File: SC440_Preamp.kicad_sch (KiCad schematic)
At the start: 24 parts, among them J1 JST-XH 1x04 TO DIGITAL BOARD, J2 ANALOG BOARD, U1 OPA1678IDR

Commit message: fix spice tool and pin assignments
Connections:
- net +5V: now also VCCSIM1.1 (+); no longer VCCSIM1.2 (-)
- net ANALOG_INPUT: now also VTEST1.1 (+); no longer VTEST1.2 (-)
- net FB: now also XAMP1.4 (-IN); no longer XAMP1.3 (+IN)
- net GND: now also VCCSIM1.2 (-), VTEST1.2 (-), XAMP1.2 (VEE), XREF1.2 (VEE); no longer VCCSIM1.1 (+), VTEST1.1 (+), XAMP1.1 (OUT), XREF1.1 (OUT)
- net IN_AC: now also XAMP1.3 (+IN); no longer XAMP1.4 (-IN)
- net PREAMP_OUT: now also XAMP1.1 (OUT); no longer XAMP1.2 (VEE)
- net VREF: now also XREF1.1 (OUT), XREF1.4 (-IN); no longer XREF1.2 (VEE), XREF1.3 (+IN)
- net VREF_RAW: now also XREF1.3 (+IN); no longer XREF1.4 (-IN)
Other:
- moved on the sheet: VCCSIM1, VTEST1
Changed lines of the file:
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@@
 	(wire
 		(pts
-			(xy 135.08 211.27) (xy 143 211.27)
+			(xy 142.365 212.54) (xy 144.27 212.54)
+		)
+		(stroke
+			(width 0)
+			(type solid)
+		)
+	)
+	(wire
+		(pts
+			(xy 142.365 211.27) (xy 135.08 211.27)
 		)
 		(stroke
@@
 	(wire
 		(pts
+			(xy 192.365 212.54) (xy 192.365 211.27)
+		)
+		(stroke
+			(width 0)
+			(type solid)
+		)
+	)
+	(wire
+		(pts
 			(xy 26.67 56.64) (xy 26.67 113.792)
 		)
@@
 	(wire
 		(pts
+			(xy 192.365 211.27) (xy 185.08 211.27)
+		)
+		(stroke
+			(width 0)
+			(type solid)
+		)
+	)
+	(wire
+		(pts
 			(xy 165.862 85.09) (xy 176.53 85.09)
 		)
@@
 	(wire
 		(pts
+			(xy 142.365 212.54) (xy 142.365 211.27)
+		)
+		(stroke
+			(width 0)
+			(type solid)
+		)
+	)
+	(wire
+		(pts
 			(xy 42.545 48.385) (xy 34.29 48.385)
 		)
@@
 	(wire
 		(pts
-			(xy 185.08 211.27) (xy 193 211.27)
+			(xy 192.365 212.54) (xy 194.27 212.54)
 		)
 		(stroke
@@
 	)
 	(label "VREF"
-		(at 193 208.73 0)
+		(at 194.27 212.54 0)
 		(effects
 			(font
@@
 	)
 	(label "IN_AC"
-		(at 117 208.73 180)
+		(at 117 211.27 180)
 		(effects
 			(font
@@
 	)
 	(label "VREF"
-		(at 167 211.27 180)
+		(at 167 208.73 180)
 		(effects
 			(font
@@
 	)
 	(label "PREAMP_OUT"
-		(at 143 208.73 0)
+		(at 144.27 212.54 0)
 		(effects
 			(font
@@
 	)
 	(label "VREF_RAW"
-		(at 167 208.73 180)
+		(at 167 211.27 180)
 		(effects
 			(font
@@
 	)
 	(label "FB"
-		(at 117 211.27 180)
+		(at 117 208.73 180)
 		(effects
 			(font
@@
 			)
 		)
-		(property "Sim.Pins" "1=4 2=5 3=2 4=1 5=3"
+		(property "Sim.Pins" "1=OUT 2=VEE 3=IN+ 4=IN- 5=VCC"
 			(at 0 0 0)
 			(hide yes)
@@
 			)
 		)
-		(property "Sim.Pins" "1=4 2=5 3=2 4=1 5=3"
+		(property "Sim.Pins" "1=OUT 2=VEE 3=IN+ 4=IN- 5=VCC"
 			(at 0 0 0)
 			(hide yes)
@@
 	(symbol
 		(lib_id "power:GND")
-		(at 193 211.27 0)
+		(at 193 208.73 90)
 		(unit 1)
 		(body_style 1)
@@
 		(fields_autoplaced yes)
 		(property "Reference" "#PWR012"
-			(at 193 217.62 0)
+			(at 199.35 208.73 0)
 			(hide yes)
 			(show_name no)
@@
 		)
 		(property "Value" "GND"
-			(at 195.58 212.5399 0)
+			(at 196.85 208.7299 90)
 			(show_name no)
 			(do_not_autoplace no)
@@
 					(size 1.27 1.27)
 				)
-				(justify left)
+				(justify right)
 			)
 		)
 		(property "Footprint" ""
-			(at 193 211.27 0)
+			(at 193 208.73 0)
 			(hide yes)
 			(show_name no)
@@
 		)
 		(property "Datasheet" ""
-			(at 193 211.27 0)
+			(at 193 208.73 0)
 			(hide yes)
 			(show_name no)
@@
 		)
 		(property "Description" "Power symbol creates a global label with name \"GND\" , ground"
-			(at 193 211.27 0)
+			(at 193 208.73 0)
 			(hide yes)
 			(show_name no)
@@
 	(symbol
 		(lib_id "power:GND")
-		(at 143 211.27 0)
+		(at 143 208.73 90)
 		(unit 1)
 		(body_style 1)
@@
 		(fields_autoplaced yes)
 		(property "Reference" "#PWR011"
-			(at 143 217.62 0)
+			(at 149.35 208.73 0)
 			(hide yes)
 			(show_name no)
@@
 		)
 		(property "Value" "GND"
-			(at 146.05 212.5399 0)
+			(at 147.32 208.7299 90)
 			(show_name no)
 			(do_not_autoplace no)
@@
 					(size 1.27 1.27)
 				)
-				(justify left)
+				(justify right)
 			)
 		)
 		(property "Footprint" ""
-			(at 143 211.27 0)
+			(at 143 208.73 0)
 			(hide yes)
 			(show_name no)
@@
 		)
 		(property "Datasheet" ""
-			(at 143 211.27 0)
+			(at 143 208.73 0)
 			(hide yes)
 			(show_name no)
@@
 		)
 		(property "Description" "Power symbol creates a global label with name \"GND\" , ground"
-			(at 143 211.27 0)
+			(at 143 208.73 0)
 			(hide yes)
 			(show_name no)
@@
 	(symbol
 		(lib_id "SC440_Preamp:VDC")
-		(at 75 210 0)
+		(at 75 210 180)
 		(unit 1)
 		(body_style 1)
@@
 					(size 1.27 1.27)
 				)
-				(justify left)
+				(justify right)
 			)
 		)
@@
 					(size 1.27 1.27)
 				)
-				(justify left)
+				(justify right)
 			)
 		)
 		(property "Footprint" ""
-			(at 75 211 0)
+			(at 75 209 0)
 			(hide yes)
 			(show_name no)
@@
 		)
 		(property "Datasheet" ""
-			(at 75 213 0)
+			(at 75 207 0)
 			(hide yes)
 			(show_name no)
@@
 			)
 		)
-		(property "Sim.Pins" "1=- 2=+"
-			(at 0 0 0)
+		(property "Sim.Pins" "1=+ 2=-"
+			(at 150 420 0)
 			(hide yes)
 			(show_name no)
@@
 		)
 		(property "Sim.Device" "V"
-			(at 0 0 0)
+			(at 150 420 0)
 			(hide yes)
 			(show_name no)
@@
 		)
 		(property "Sim.Type" "DC"
-			(at 0 0 0)
+			(at 150 420 0)
 			(hide yes)
 			(show_name no)
@@
 		)
 		(property "Sim.Params" "dc=5"
-			(at 0 0 0)
+			(at 150 420 0)
 			(hide yes)
 			(show_name no)
@@
 	(symbol
 		(lib_id "SC440_Preamp:VSIN")
-		(at 45 210 0)
+		(at 45 210 180)
 		(unit 1)
 		(body_style 1)
@@
 					(size 1.27 1.27)
 				)
-				(justify left)
+				(justify right)
 			)
 		)
@@
 					(size 1.27 1.27)
 				)
-				(justify left)
+				(justify right)
 			)
 		)
 		(property "Footprint" ""
-			(at 45 211 0)
+			(at 45 209 0)
 			(hide yes)
 			(show_name no)
@@
 		)
 		(property "Datasheet" ""
-			(at 45 213 0)
+			(at 45 207 0)
 			(hide yes)
 			(show_name no)
@@
 			)
 		)
-		(property "Sim.Pins" "1=- 2=+"
-			(at 0 0 0)
+		(property "Sim.Pins" "1=+ 2=-"
+			(at 90 420 0)
 			(hide yes)
 			(show_name no)
@@
 		)
 		(property "Sim.Device" "V"
-			(at 0 0 0)
+			(at 90 420 0)
 			(hide yes)
 			(show_name no)
@@
 		)
 		(property "Sim.Type" "SIN"
-			(at 0 0 0)
+			(at 90 420 0)
 			(hide yes)
 			(show_name no)
@@
 		)
 		(property "Sim.Params" "dc=2.426 ampl=10m f=1k ac=1"
-			(at 0 0 0)
+			(at 90 420 0)
 			(hide yes)
 			(show_name no)

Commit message: ...
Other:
- moved on the sheet: J2, XAMP1, XREF1

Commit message: add input and output filter
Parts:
- added C5: 330p, Capacitor_SMD:C_0805_2012Metric_Pad1.18x1.45mm_HandSolder, symbol SC440_Preamp:C
- added C7: 1n, Capacitor_SMD:C_0805_2012Metric_Pad1.18x1.45mm_HandSolder, symbol SC440_Preamp:C
- added R4: 1k, Resistor_SMD:R_0805_2012Metric_Pad1.20x1.40mm_HandSolder, symbol SC440_Preamp:R
- R8: now not fitted
- R8: renamed from R10; now fitted
- renumbered C5 to C6, C6 to C8, R11 to R10, R4 to R2, R2 to R5, R5 to R6, R6 to R9
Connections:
- net ANALOG_OUTPUT: now also C7.1
- net GND: now also C5.2, C7.2
- net IN_AC: now also C5.1, R4.2; no longer C2.2, R2.2
- new net: C2.2, R2.2, R4.1

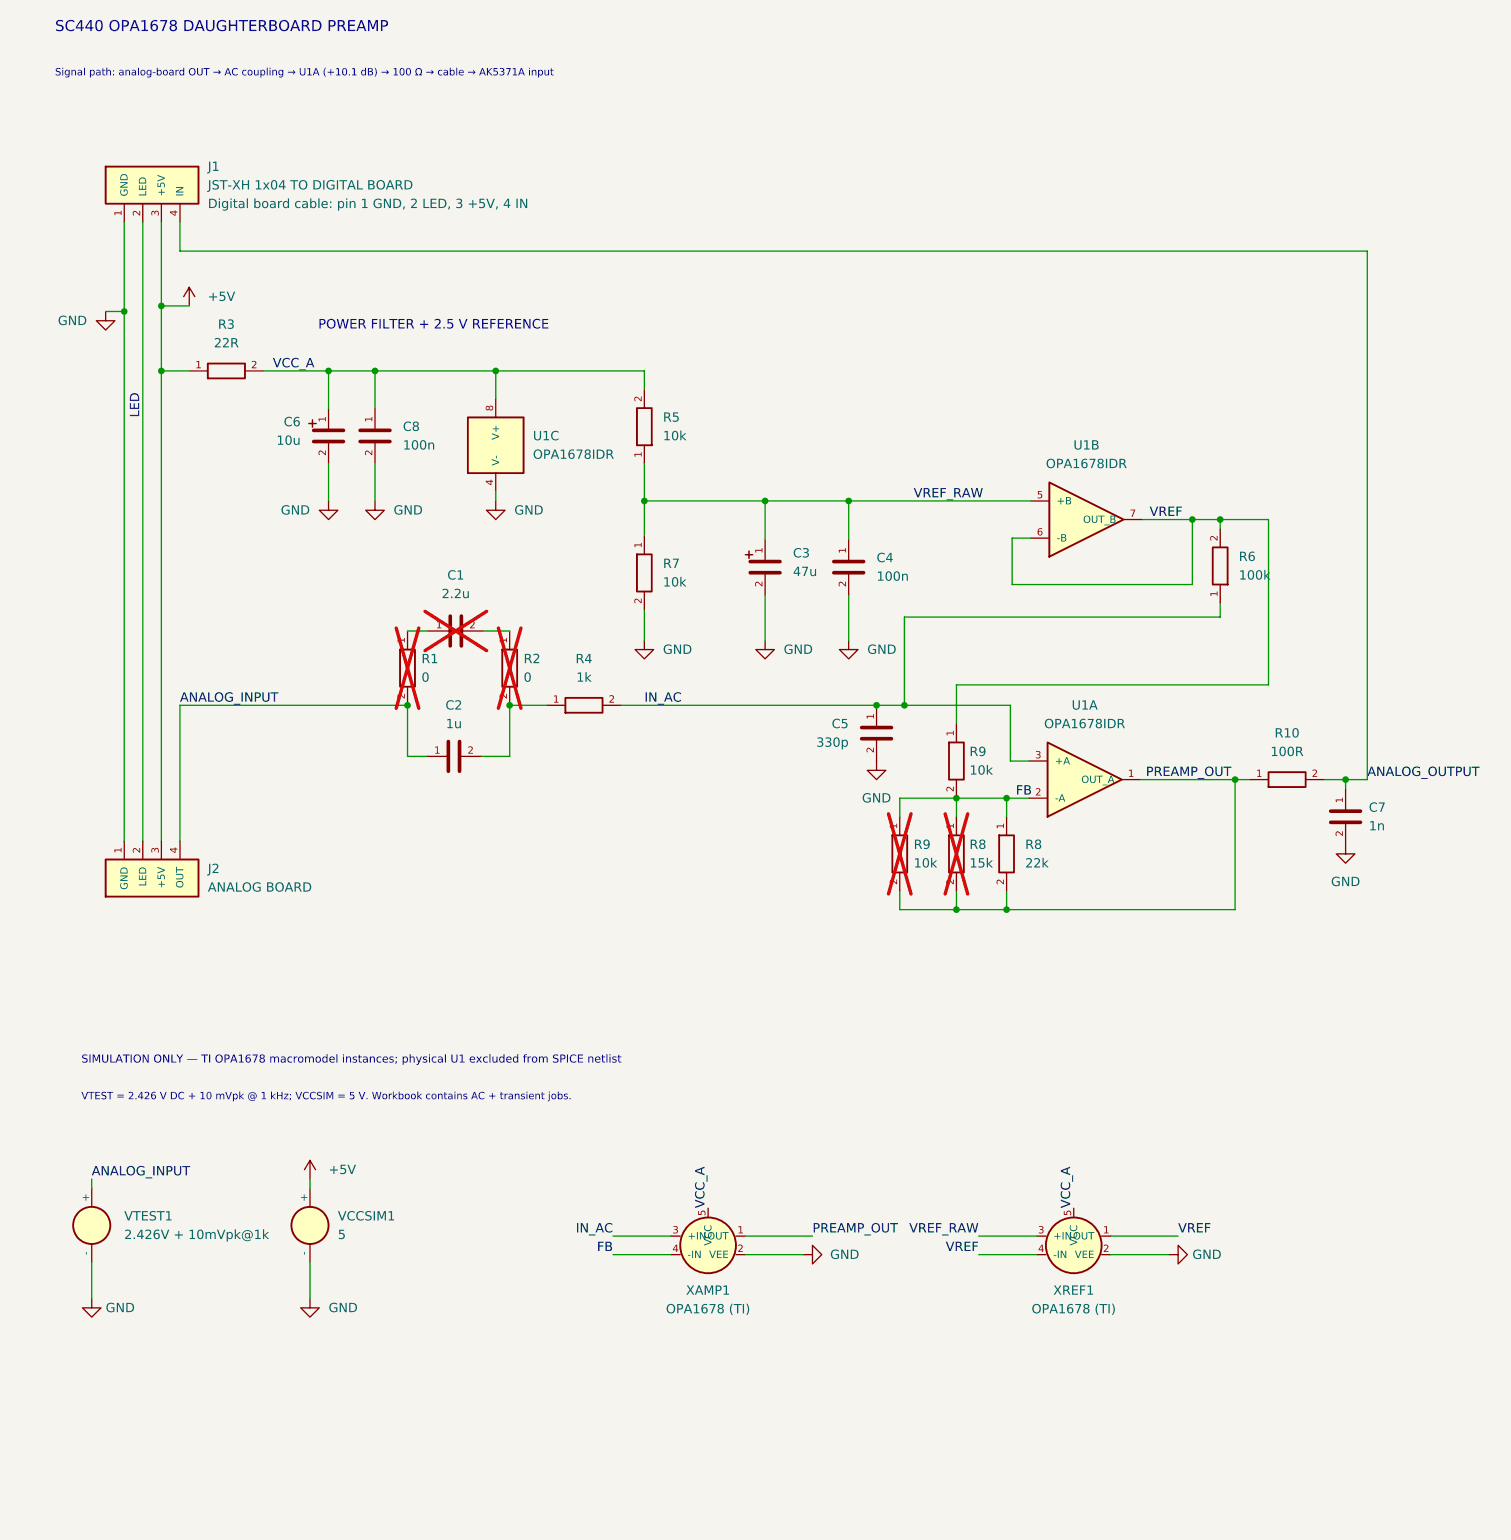
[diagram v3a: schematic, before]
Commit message: add more filtering, silkscreen, pinsockets as spacers
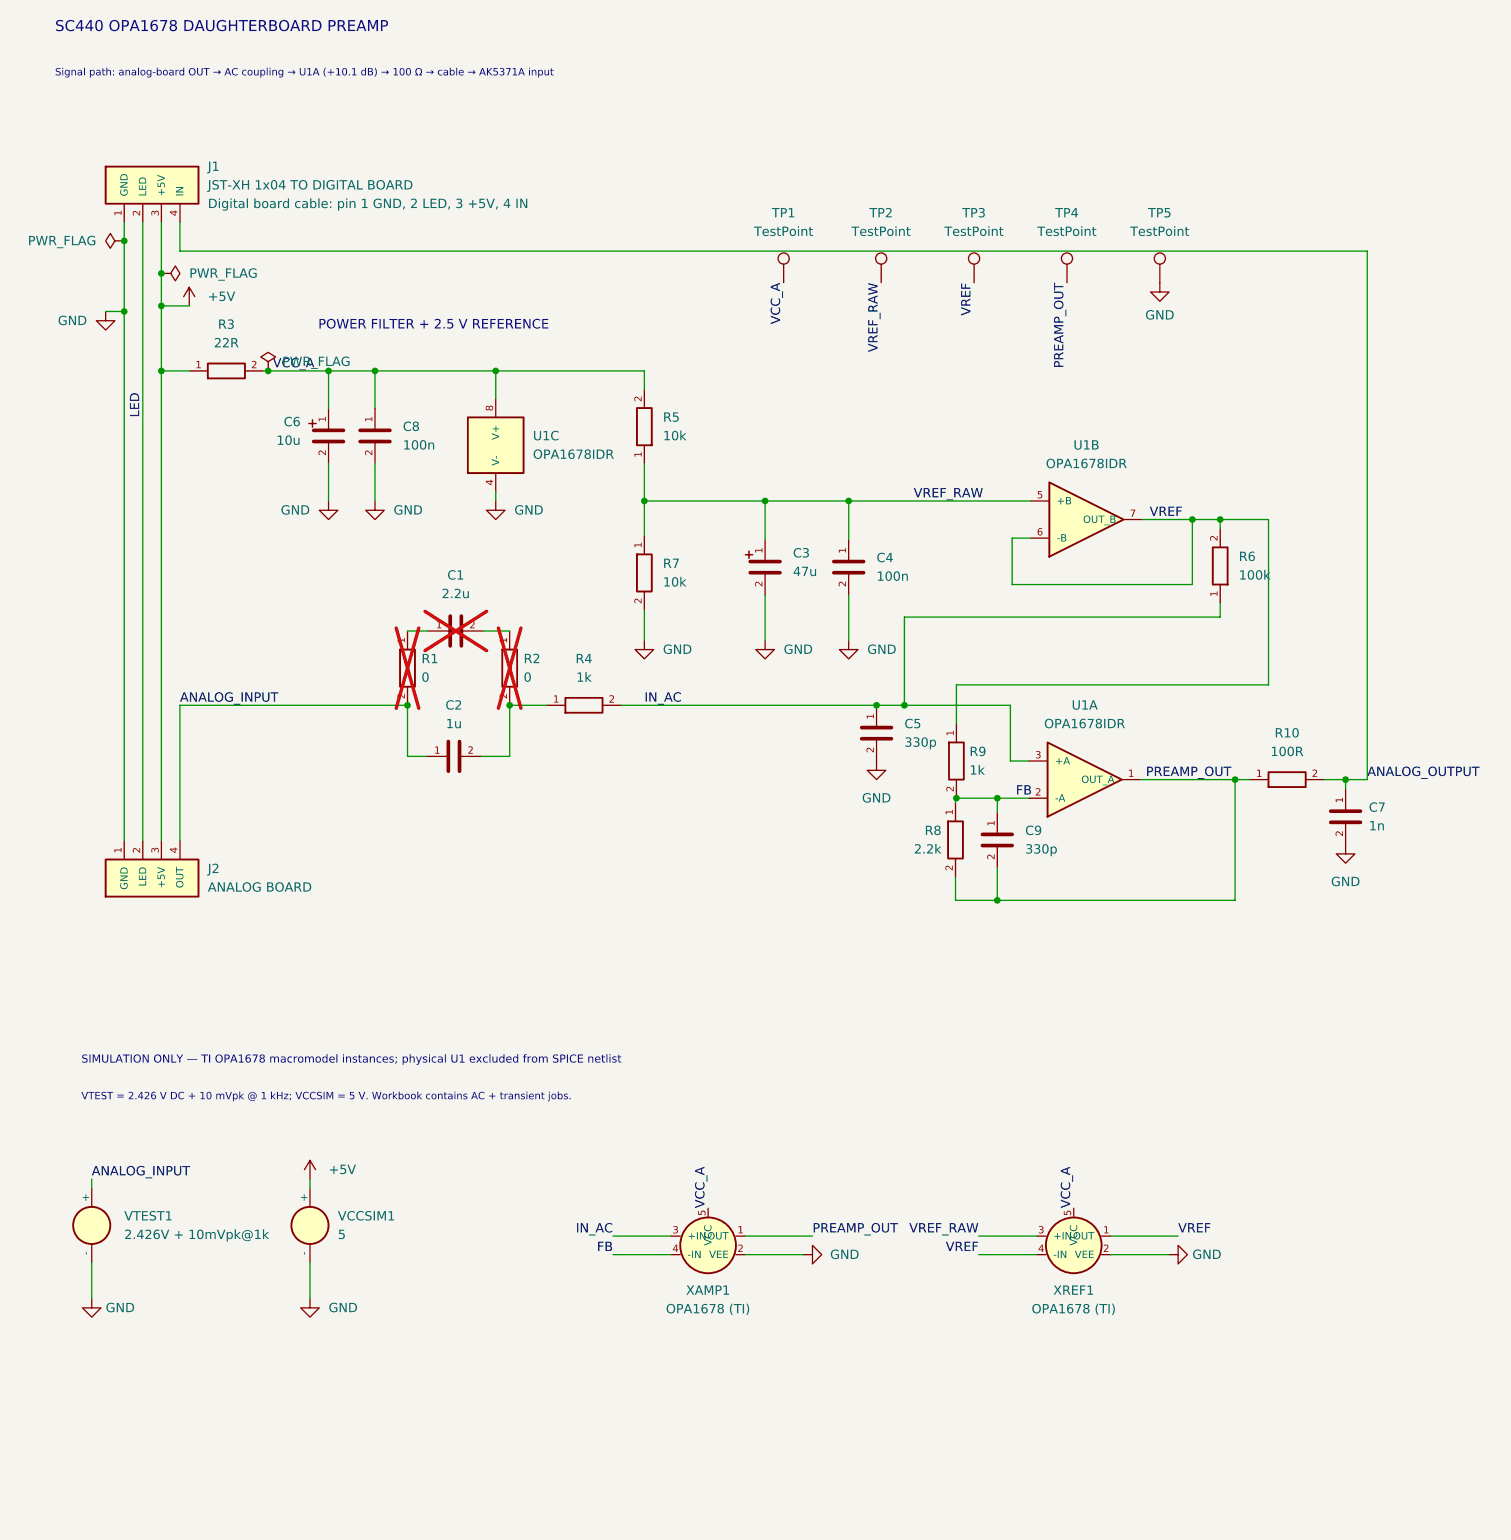
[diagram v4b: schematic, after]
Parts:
- removed R8: 15k, Resistor_SMD:R_0805_2012Metric_Pad1.20x1.40mm_HandSolder, symbol SC440_Preamp:R
- removed R9: 10k, Resistor_SMD:R_0805_2012Metric_Pad1.20x1.40mm_HandSolder, symbol SC440_Preamp:R
- added C9: 330p, Capacitor_SMD:C_0805_2012Metric_Pad1.18x1.45mm_HandSolder, symbol SC440_Preamp:C
- added TP1, TP2, TP3, TP4, TP5: TestPoint, TestPoint:TestPoint_THTPad_1.0x1.0mm_Drill0.5mm, symbol Connector:TestPoint
- C4, C8: now left out of the parts list
- R8: value 22k -> 2.2k
- R9: value 10k -> 1k
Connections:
- net FB: now also C9.1
- net GND: now also TP5.1
- net PREAMP_OUT: now also C9.2, TP4.1
- net VCC_A: now also TP1.1
- net VREF: now also TP3.1
- net VREF_RAW: now also TP2.1
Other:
- moved on the sheet: R8
